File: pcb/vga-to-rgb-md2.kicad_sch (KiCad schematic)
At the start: 11 parts, among them J1 DE15_Plug_HighDensity, J2 AudioJack3, J3 MD-90SM, U1 SN74HCS7266PWR

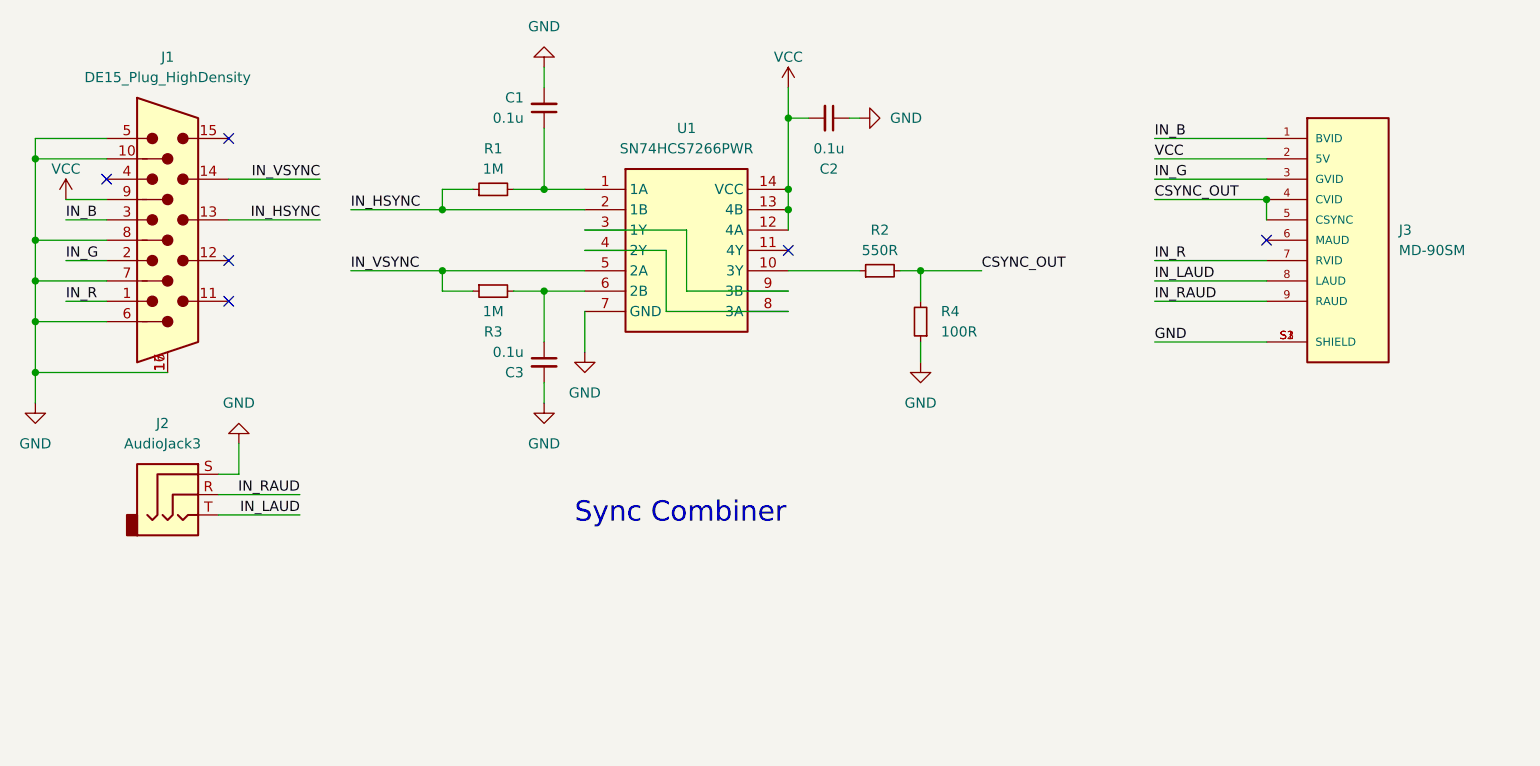
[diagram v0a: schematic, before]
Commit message: Adds external 5V
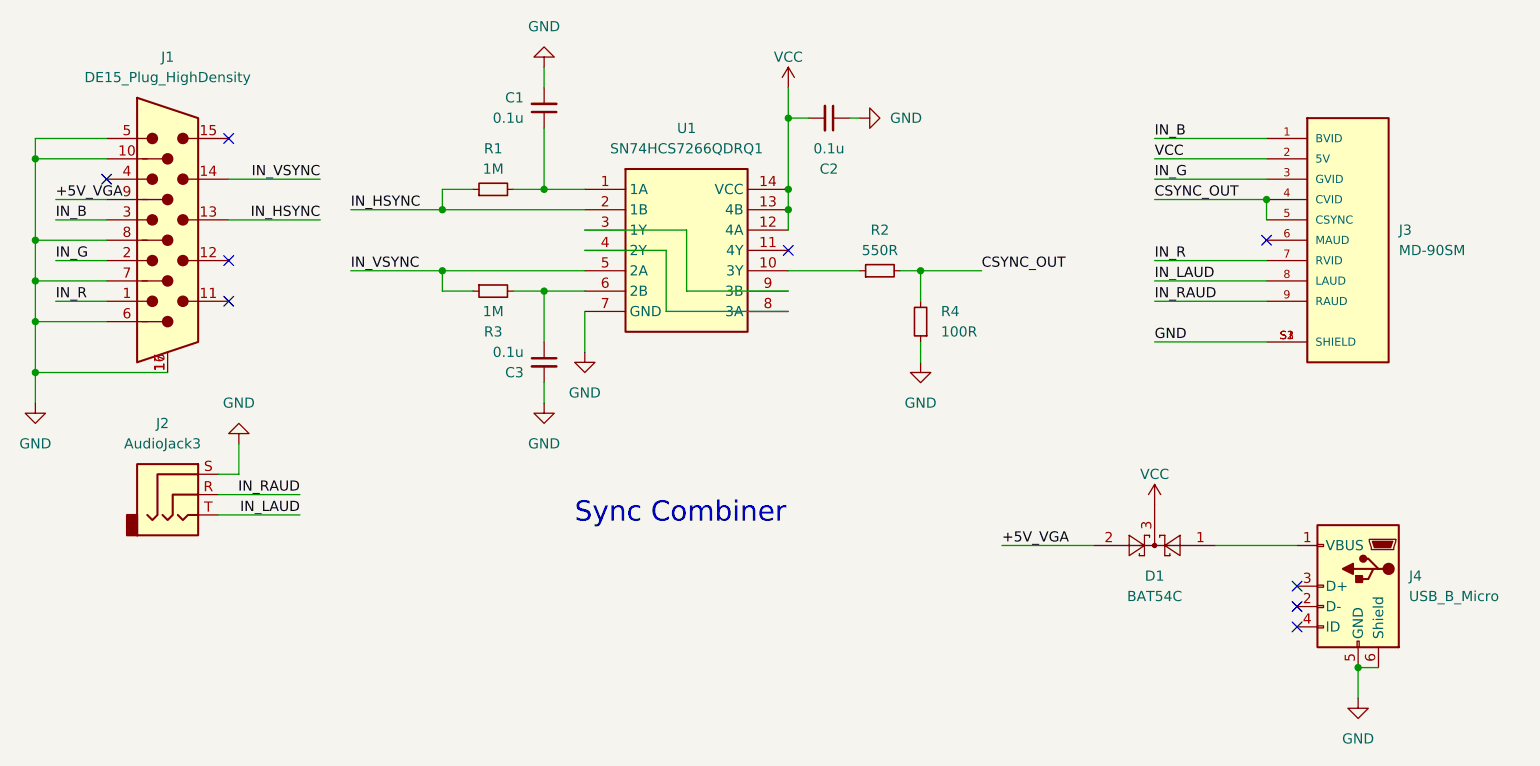
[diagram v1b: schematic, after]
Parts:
- added D1: BAT54C, Package_TO_SOT_SMD:SOT-23, symbol Diode:BAT54C
- added J4: USB_B_Micro, Connector_USB:USB_Micro-B_Molex-105017-0001, symbol Connector:USB_B_Micro
- U1: value SN74HCS7266PWR -> SN74HCS7266QDRQ1; footprint Package_SO:TSSOP-14_4.4x5mm_P0.65mm -> Package_SO:SOIC-14_3.9x8.7mm_P1.27mm
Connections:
- net GND: now also J4.5 (GND), J4.6 (Shield)
- net VCC: now also D1.3; no longer J1.9
- new net: D1.1, J4.1 (VBUS)
- new net +5V_VGA: D1.2, J1.9
- no-connect marks 6 -> 9
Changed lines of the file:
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@@
   (junction (at 124.46 41.91) (diameter 0) (color 0 0 0 0)
   )
+  (junction (at 195.58 101.6) (diameter 0) (color 0 0 0 0)
+  )
   (junction (at 93.98 41.91) (diameter 0) (color 0 0 0 0)
   )
@@
   )
   (no_connect (at 184.15 48.26))
+  (no_connect (at 187.96 93.98))
+  (no_connect (at 187.96 96.52))
+  (no_connect (at 187.96 91.44))
   (no_connect (at 39.37 40.64))
   (no_connect (at 54.61 35.56))
@@
     (stroke (width 0) (type default))
   )
-  (wire (pts (xy 34.29 45.72) (xy 39.37 45.72))
+  (wire (pts (xy 33.02 45.72) (xy 39.37 45.72))
     (stroke (width 0) (type default))
   )
@@
     (stroke (width 0) (type default))
   )
-  (wire (pts (xy 34.29 55.88) (xy 39.37 55.88))
+  (wire (pts (xy 33.02 55.88) (xy 39.37 55.88))
     (stroke (width 0) (type default))
   )
@@
     (stroke (width 0) (type default))
   )
+  (wire (pts (xy 198.12 101.6) (xy 195.58 101.6))
+    (stroke (width 0) (type default))
+  )
   (wire (pts (xy 170.18 35.56) (xy 184.15 35.56))
     (stroke (width 0) (type default))
@@
     (stroke (width 0) (type default))
   )
-  (wire (pts (xy 34.29 50.8) (xy 39.37 50.8))
+  (wire (pts (xy 33.02 50.8) (xy 39.37 50.8))
     (stroke (width 0) (type default))
   )
@@
     (stroke (width 0) (type default))
   )
-  (wire (pts (xy 39.37 43.18) (xy 34.29 43.18))
+  (wire (pts (xy 39.37 43.18) (xy 33.02 43.18))
     (stroke (width 0) (type default))
   )
@@
     (stroke (width 0) (type default))
   )
+  (wire (pts (xy 195.58 101.6) (xy 195.58 105.41))
+    (stroke (width 0) (type default))
+  )
   (wire (pts (xy 30.48 58.42) (xy 30.48 64.77))
     (stroke (width 0) (type default))
@@
     (stroke (width 0) (type default))
   )
+  (wire (pts (xy 151.13 86.36) (xy 162.56 86.36))
+    (stroke (width 0) (type default))
+  )
   (wire (pts (xy 109.22 57.15) (xy 124.46 57.15))
     (stroke (width 0) (type default))
@@
   )
   (wire (pts (xy 170.18 43.18) (xy 184.15 43.18))
+    (stroke (width 0) (type default))
+  )
+  (wire (pts (xy 177.8 86.36) (xy 187.96 86.36))
     (stroke (width 0) (type default))
   )
@@
     (effects (font (size 1.27 1.27)) (justify left bottom))
   )
+  (label "+5V_VGA" (at 33.02 43.18 0) (fields_autoplaced)
+    (effects (font (size 1.27 1.27)) (justify left bottom))
+  )
   (label "IN_RAUD" (at 170.18 55.88 0) (fields_autoplaced)
     (effects (font (size 1.27 1.27)) (justify left bottom))
   )
-  (label "IN_B" (at 34.29 45.72 0) (fields_autoplaced)
+  (label "IN_B" (at 33.02 45.72 0) (fields_autoplaced)
     (effects (font (size 1.27 1.27)) (justify left bottom))
   )
@@
     (effects (font (size 1.27 1.27)) (justify right bottom))
   )
-  (label "IN_R" (at 34.29 55.88 0) (fields_autoplaced)
-    (effects (font (size 1.27 1.27)) (justify left bottom))
-  )
-  (label "IN_G" (at 34.29 50.8 0) (fields_autoplaced)
+  (label "IN_R" (at 33.02 55.88 0) (fields_autoplaced)
+    (effects (font (size 1.27 1.27)) (justify left bottom))
+  )
+  (label "+5V_VGA" (at 151.13 86.36 0) (fields_autoplaced)
+    (effects (font (size 1.27 1.27)) (justify left bottom))
+  )
+  (label "IN_G" (at 33.02 50.8 0) (fields_autoplaced)
     (effects (font (size 1.27 1.27)) (justify left bottom))
   )
@@
       (effects (font (size 1.27 1.27)))
     )
-    (property "Value" "SN74HCS7266PWR" (at 111.76 36.83 0)
-      (effects (font (size 1.27 1.27)))
-    )
-    (property "Footprint" "Package_SO:TSSOP-14_4.4x5mm_P0.65mm" (at 120.65 136.83 0)
+    (property "Value" "SN74HCS7266QDRQ1" (at 111.76 36.83 0)
+      (effects (font (size 1.27 1.27)))
+    )
+    (property "Footprint" "Package_SO:SOIC-14_3.9x8.7mm_P1.27mm" (at 120.65 136.83 0)
       (effects (font (size 1.27 1.27)) (justify left top) hide)
     )
@@
     )
   )
+  (symbol (lib_id "Diode:BAT54C") (at 170.18 86.36 180) (unit 1)
+    (in_bom yes) (on_board yes) (dnp no) (fields_autoplaced)
+    (property "Reference" "D1" (at 170.18 90.17 0)
+      (effects (font (size 1.27 1.27)))
+    )
+    (property "Value" "BAT54C" (at 170.18 92.71 0)
+      (effects (font (size 1.27 1.27)))
+    )
+    (property "Footprint" "Package_TO_SOT_SMD:SOT-23" (at 168.275 89.535 0)
+      (effects (font (size 1.27 1.27)) (justify left) hide)
+    )
+    (property "Datasheet" "http://www.diodes.com/_files/datasheets/ds11005.pdf" (at 172.212 86.36 0)
+      (effects (font (size 1.27 1.27)) hide)
+    )
+    (pin "1")
+    (pin "2")
+    (pin "3")
+    (instances
+      (project "vga-to-rgb-md2"
+        (path "/f8bf2a67-b621-4cb9-9f90-407d179e32a5"
+          (reference "D1") (unit 1)
+        )
+      )
+    )
+  )
+  (symbol (lib_id "power:GND") (at 195.58 105.41 0) (unit 1)
+    (in_bom yes) (on_board yes) (dnp no) (fields_autoplaced)
+    (property "Reference" "#PWR010" (at 195.58 111.76 0)
+      (effects (font (size 1.27 1.27)) hide)
+    )
+    (property "Value" "GND" (at 195.58 110.49 0)
+      (effects (font (size 1.27 1.27)))
+    )
+    (property "Footprint" "" (at 195.58 105.41 0)
+      (effects (font (size 1.27 1.27)) hide)
+    )
+    (property "Datasheet" "" (at 195.58 105.41 0)
+      (effects (font (size 1.27 1.27)) hide)
+    )
+    (pin "1")
+    (instances
+      (project "vga-to-rgb-md2"
+        (path "/f8bf2a67-b621-4cb9-9f90-407d179e32a5"
+          (reference "#PWR010") (unit 1)
+        )
+      )
+    )
+  )
   (symbol (lib_id "power:GND") (at 133.35 33.02 90) (unit 1)
     (in_bom yes) (on_board yes) (dnp no) (fields_autoplaced)
@@
     )
   )
+  (symbol (lib_id "Connector:USB_B_Micro") (at 195.58 91.44 0) (mirror y) (unit 1)
+    (in_bom yes) (on_board yes) (dnp no) (fields_autoplaced)
+    (property "Reference" "J4" (at 201.93 90.17 0)
+      (effects (font (size 1.27 1.27)) (justify right))
+    )
+    (property "Value" "USB_B_Micro" (at 201.93 92.71 0)
+      (effects (font (size 1.27 1.27)) (justify right))
+    )
+    (property "Footprint" "Connector_USB:USB_Micro-B_Molex-105017-0001" (at 191.77 92.71 0)
+      (effects (font (size 1.27 1.27)) hide)
+    )
+    (property "Datasheet" "~" (at 191.77 92.71 0)
+      (effects (font (size 1.27 1.27)) hide)
+    )
+    (property "Notes" "" (at 195.58 91.44 0)
+      (effects (font (size 1.27 1.27)))
+    )
+    (pin "1")
+    (pin "2")
+    (pin "3")
+    (pin "4")
+    (pin "5")
+    (pin "6")
+    (instances
+      (project "vga-to-rgb-md2"
+        (path "/f8bf2a67-b621-4cb9-9f90-407d179e32a5"
+          (reference "J4") (unit 1)
+        )
+      )
+    )
+  )
   (symbol (lib_id "power:GND") (at 140.97 63.5 0) (unit 1)
     (in_bom yes) (on_board yes) (dnp no) (fields_autoplaced)
@@
         (path "/f8bf2a67-b621-4cb9-9f90-407d179e32a5"
           (reference "#PWR06") (unit 1)
+        )
+      )
+    )
+  )
+  (symbol (lib_id "power:VCC") (at 170.18 81.28 0) (unit 1)
+    (in_bom yes) (on_board yes) (dnp no)
+    (property "Reference" "#PWR03" (at 170.18 85.09 0)
+      (effects (font (size 1.27 1.27)) hide)
+    )
+    (property "Value" "VCC" (at 170.18 77.47 0)
+      (effects (font (size 1.27 1.27)))
+    )
+    (property "Footprint" "" (at 170.18 81.28 0)
+      (effects (font (size 1.27 1.27)) hide)
+    )
+    (property "Datasheet" "" (at 170.18 81.28 0)
+      (effects (font (size 1.27 1.27)) hide)
+    )
+    (pin "1")
+    (instances
+      (project "vga-to-rgb-md2"
+        (path "/f8bf2a67-b621-4cb9-9f90-407d179e32a5"
+          (reference "#PWR03") (unit 1)
         )
       )
@@
         )
       )
-    )
-  )
-  (symbol (lib_id "power:VCC") (at 34.29 43.18 0) (unit 1)
-    (in_bom yes) (on_board yes) (dnp no)
-    (property "Reference" "#PWR03" (at 34.29 46.99 0)
-      (effects (font (size 1.27 1.27)) hide)
-    )
-    (property "Value" "VCC" (at 34.29 39.37 0)
-      (effects (font (size 1.27 1.27)))
-    )
-    (property "Footprint" "" (at 34.29 43.18 0)
-      (effects (font (size 1.27 1.27)) hide)
-    )
-    (property "Datasheet" "" (at 34.29 43.18 0)
-      (effects (font (size 1.27 1.27)) hide)
-    )
-    (pin "1")
-    (instances
-      (project "vga-to-rgb-md2"
-        (path "/f8bf2a67-b621-4cb9-9f90-407d179e32a5"
-          (reference "#PWR03") (unit 1)
-        )
-      )
